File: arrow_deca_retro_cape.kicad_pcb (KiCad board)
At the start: 4 copper layers, 78.6 x 100 mm, 30 parts, among them J1 ZXSP_ED2X28_SPE_SOL_EDGE, J10 Conn_02x05_Odd_Even, J12 Conn_01x03, J13 Conn_01x01, J14 Conn_01x02, J15 Conn_01x03, J16 Conn_01x06, J2 Conn_01x03, J4 DB9_Male, J5 DINC_MIN_TM_6_1, J6 Conn_02x20_Odd_Even, J7 Conn_01x03, J8 P8_Male, J9 P9_Male, U4 LM1117-3.3, U5 LM1117-2.5

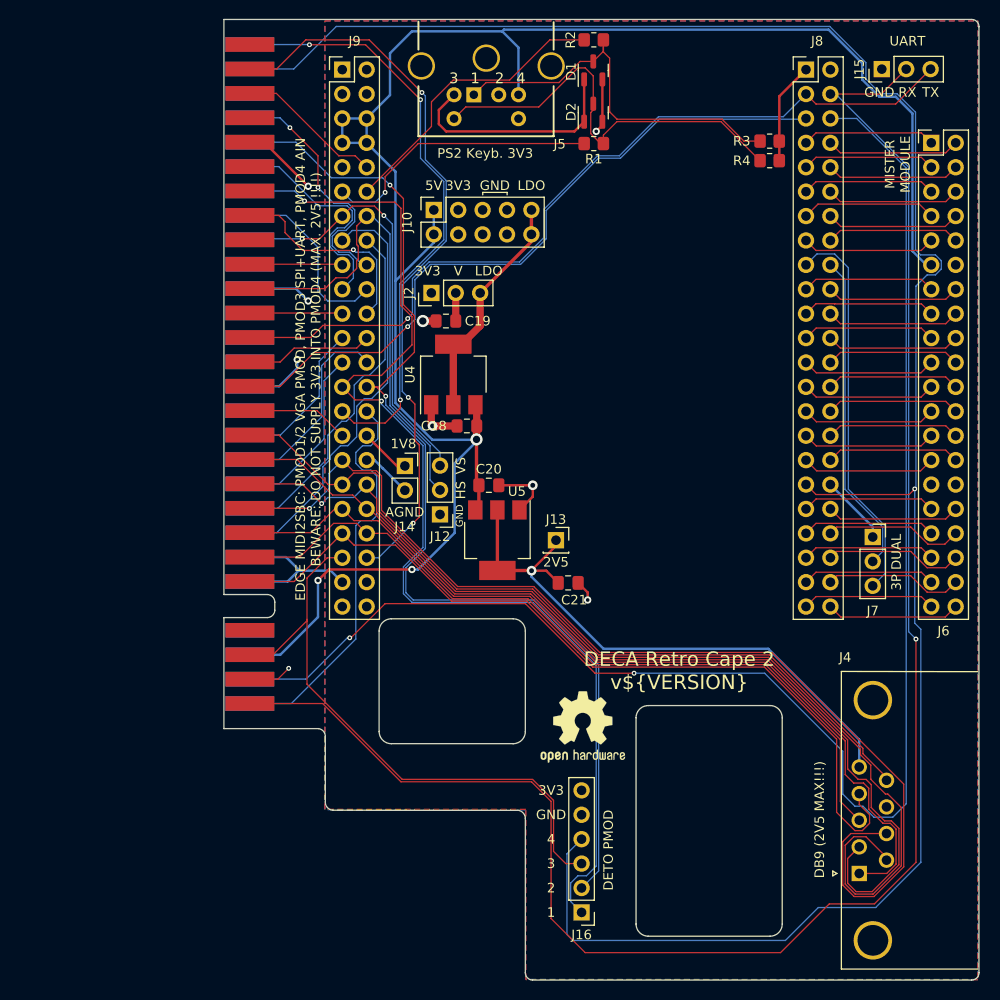
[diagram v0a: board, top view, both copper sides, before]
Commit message: v0.61 2-layer. Edge removed
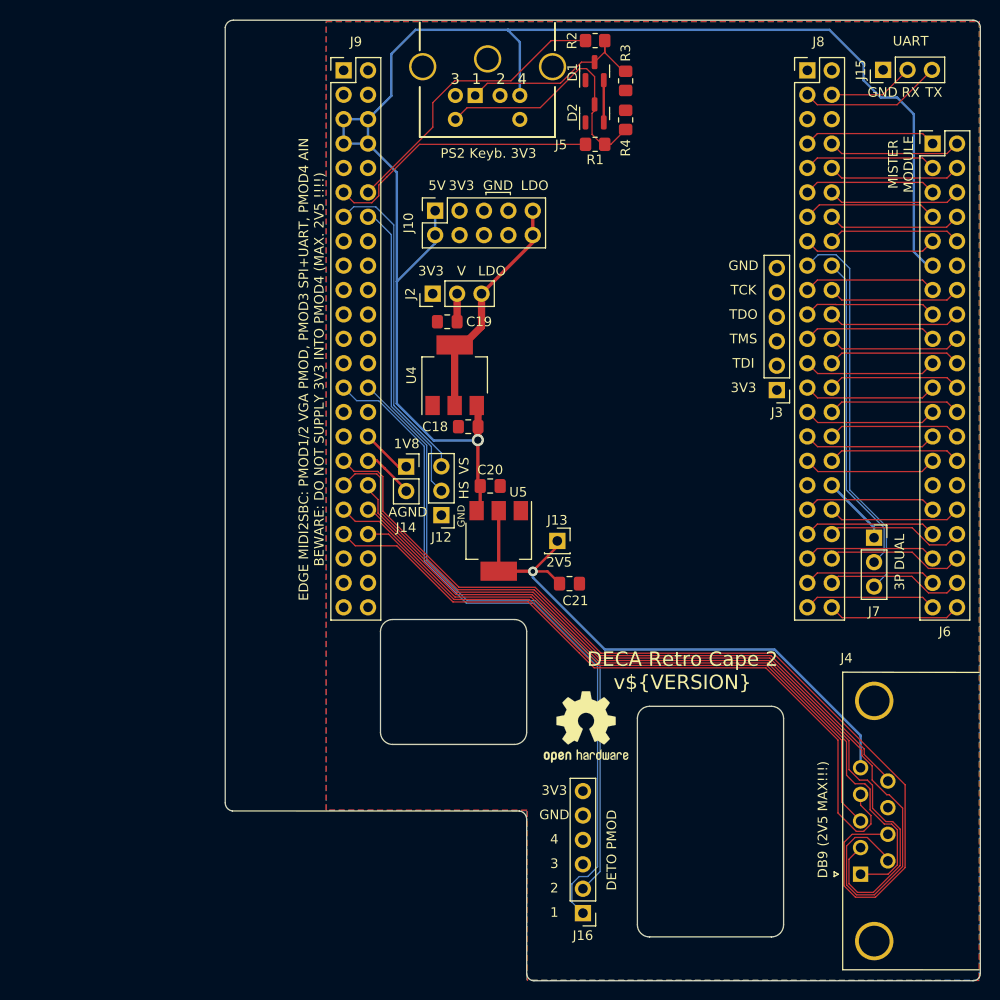
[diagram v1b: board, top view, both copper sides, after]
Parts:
- removed J1: ZXSP_ED2X28_SPE_SOL_EDGE, addon-edge-rpi-i2s-pmod:2X28_SPE2
- added J3: Conn_01x06, Connector_PinHeader_2.54mm:PinHeader_1x06_P2.54mm_Vertical, F.Cu at (161.9, 79.0)
- moved R3 16.2 mm to (146.2, 46.8), turned to -90 degrees
- moved R4 15.6 mm to (146.2, 50.9), turned to 90 degrees
- moved LO2 0.34 mm to (142.1, 114.0)
- moved C21 0.16 mm to (140.3, 99.1)
- moved J13 0.16 mm to (139.1, 94.7)
- moved J16 0.16 mm to (141.7, 133.4)
- moved C19 0.16 mm to (127.6, 71.9)
- moved J10 0.16 mm to (126.4, 60.3)
- moved J12 0.16 mm to (127.0, 92.0)
- moved J14 0.16 mm to (123.4, 87.0)
- moved J2 0.16 mm to (126.1, 69.0)
- moved J9 0.16 mm to (116.8, 45.7)
- moved C18 0.16 mm to (129.8, 82.8)
- moved C20 0.16 mm to (132.1, 89.0)
- moved D1 0.16 mm to (143.0, 45.8)
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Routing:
- net GND: track 477.2 -> 0.00 mm, vias 5 -> 0
- net /DETO4: track 220.8 -> 0.00 mm, vias 1 -> 0
- net /UART_RXD: track 184.0 -> 8.96 mm, vias 1 -> 0
- net /SPI_CS_IO: track 160.1 -> 0.00 mm, vias 2 -> 0
- net +3V3: track 159.8 -> 7.32 mm, vias 2 -> 0
- net /SPI_CS_FPGA: track 76.5 -> 0.00 mm, vias 3 -> 0
- net /SPI_CS_OSD: track 73.6 -> 0.00 mm, vias 1 -> 0
- net /UART_TXD: track 87.1 -> 14.9 mm, vias 1 -> 0
- net +2V5: track 130.6 -> 62.3 mm, vias 2 -> 1
- net /DETO3: track 62.6 -> 0.00 mm
- net /SPI_DI (MISO): track 62.3 -> 0.00 mm, vias 3 -> 0
- net /PS2_MOUSE_DAT: track 61.0 -> 0.00 mm, vias 1 -> 0
- net /DETO2: track 113.9 -> 67.1 mm, vias 2 -> 0
- net /DETO1: track 118.6 -> 73.2 mm, vias 2 -> 0
- net /VGA_B0: track 44.3 -> 0.00 mm
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- removed copper zone on In2.Cu, net +3V3
- removed copper zone on In1.Cu, net GND
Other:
- outline, holes or cut-outs redrawn
- copper layers 4 -> 2
- board text added: "TCK"
- board text added: "TDI"
- board text added: "TDO"
- board text added: "TMS"
- board text added: "https://github.com/somhi/DECA_retro_cape_2"
- board text removed: "0.1270 mm"
- board text removed: "0.1270 mm / 0.0000 mm"
- board text removed: "1.6000 mm"
- board text removed: "78.6332 mm x 100.0130 mm"
- board text removed: "BOARD CHARACTERISTICS"
- board text removed: "Board Thickness:"
- board text removed: "Board overall dimensions:"
- board text removed: "Castellated pads:"
- board text removed: "Copper Finish:"
- board text removed: "Copper Layer Count:"
- board text removed: "DECA Retro Cape 1 v${VERSION}"
- board text removed: "Edge card connectors:"
- board text removed: "Impedance Control:"
- board text removed: "Min hole diameter:"
- board text removed: "Min track/spacing:"
- board text removed: "No"
- board text removed: "None"
- board text removed: "Plated Board Edge:"
- board text removed: "https://github.com/somhi/DECA_retro_cape_1"

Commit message: v0.62 only vga routing missing
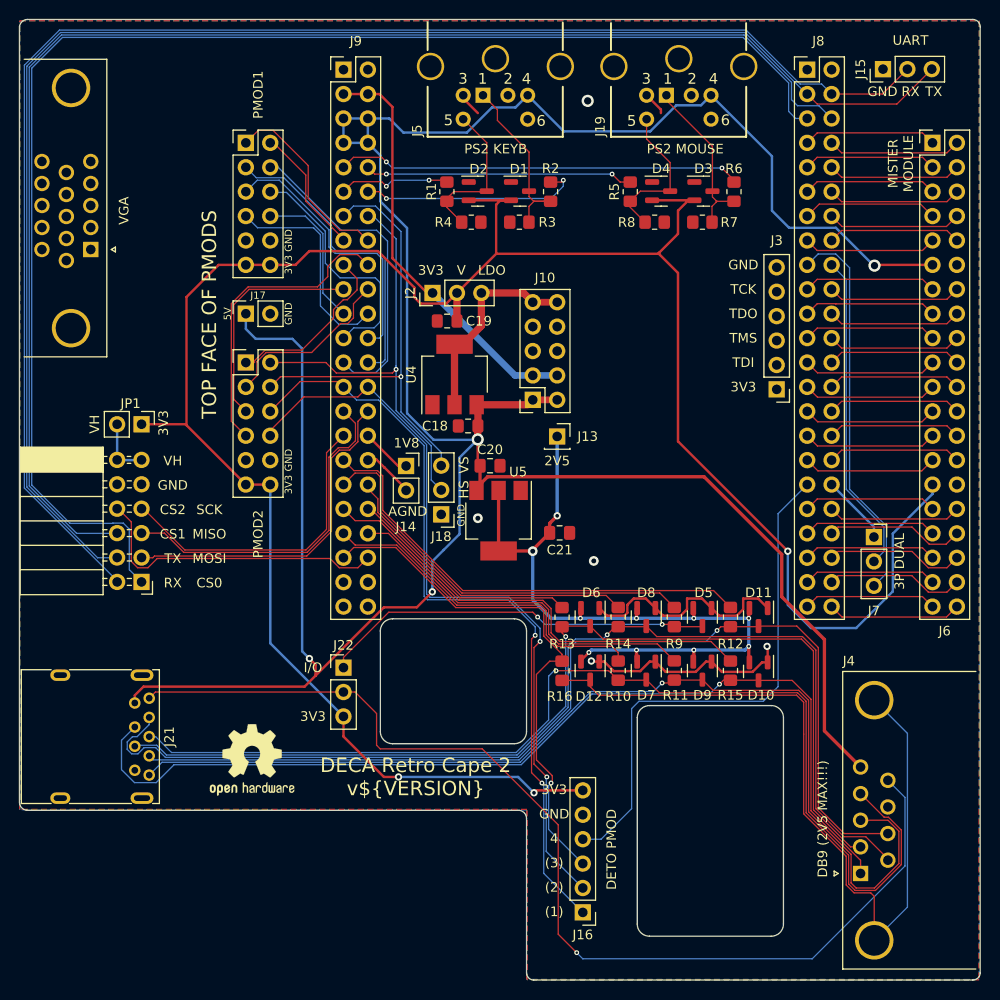
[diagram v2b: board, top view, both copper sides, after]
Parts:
- added D10: BAT54S, Package_TO_SOT_SMD:SOT-23, F.Cu at (160.0, 108.3)
- added D11: BAT54S, Package_TO_SOT_SMD:SOT-23, F.Cu at (160.0, 102.6)
- added D12: BAT54S, Package_TO_SOT_SMD:SOT-23, F.Cu at (142.5, 108.2)
- added D3: BAT54S, Package_TO_SOT_SMD:SOT-23, F.Cu at (154.3, 58.3)
- added D4: BAT54S, Package_TO_SOT_SMD:SOT-23, F.Cu at (149.9, 58.3)
- added D5: BAT54S, Package_TO_SOT_SMD:SOT-23, F.Cu at (154.2, 102.6)
- added D6: BAT54S, Package_TO_SOT_SMD:SOT-23, F.Cu at (142.5, 102.6)
- added D7: BAT54S, Package_TO_SOT_SMD:SOT-23, F.Cu at (148.3, 108.2)
- added D8: BAT54S, Package_TO_SOT_SMD:SOT-23, F.Cu at (148.3, 102.6)
- added D9: BAT54S, Package_TO_SOT_SMD:SOT-23, F.Cu at (154.2, 108.2)
- added J1: DB15_Female_HighDensity, vga:DSUB-15-HD_Female_Horizontal_P2.29x2.54mm_EdgePinOffset3.03mm_Housed_MountingHolesOffset4.94mm, F.Cu at (90.5, 64.4)
- added J11: PMOD1, addon-edge-rpi-i2s-pmod:Pmod_2x06_P2.54mm_Vertical_2, F.Cu at (106.7, 53.3)
- added J12: PMOD2, addon-edge-rpi-i2s-pmod:Pmod_2x06_P2.54mm_Vertical_2, F.Cu at (106.7, 76.1)
- added J17: Conn_01x02, Connector_PinSocket_2.54mm:PinSocket_1x02_P2.54mm_Vertical, F.Cu at (106.7, 71.0)
- added J19: DINC_MIN_TM_6_1, ps2:DINC_MIN_TM_6_1PRIMARY, F.Cu at (151.7, 39.8)
- added J20: PMOD3, addon-edge-rpi-i2s-pmod:PMOD_Female_Horizontal_2, F.Cu at (95.8, 86.3)
- added J21: USB3_A, Connector_USB:USB3_A_Molex_48393-001, F.Cu at (95.1, 111.6)
- added J22: Conn_01x03, Connector_PinHeader_2.54mm:PinHeader_1x03_P2.54mm_Vertical, F.Cu at (116.8, 107.9)
- added JP1: Conn_01x02, Connector_PinHeader_2.54mm:PinHeader_1x02_P2.54mm_Vertical, F.Cu at (95.8, 82.5)
- added R10: 100, Resistor_SMD:R_0805_2012Metric_Pad1.20x1.40mm_HandSolder, F.Cu at (145.4, 108.2)
- added R11: 100, Resistor_SMD:R_0805_2012Metric_Pad1.20x1.40mm_HandSolder, F.Cu at (151.3, 108.2)
- added R12: 100, Resistor_SMD:R_0805_2012Metric_Pad1.20x1.40mm_HandSolder, F.Cu at (157.1, 102.6)
- added R13: 100, Resistor_SMD:R_0805_2012Metric_Pad1.20x1.40mm_HandSolder, F.Cu at (139.6, 102.6)
- added R14: 100, Resistor_SMD:R_0805_2012Metric_Pad1.20x1.40mm_HandSolder, F.Cu at (145.4, 102.6)
- added R15: 100, Resistor_SMD:R_0805_2012Metric_Pad1.20x1.40mm_HandSolder, F.Cu at (157.1, 108.2)
- added R16: 100, Resistor_SMD:R_0805_2012Metric_Pad1.20x1.40mm_HandSolder, F.Cu at (139.6, 108.2)
- added R5: 120, Resistor_SMD:R_0805_2012Metric_Pad1.20x1.40mm_HandSolder, F.Cu at (146.7, 58.3)
- added R6: 120, Resistor_SMD:R_0805_2012Metric_Pad1.20x1.40mm_HandSolder, F.Cu at (157.5, 58.3)
- added R7: DNI, Resistor_SMD:R_0805_2012Metric_Pad1.20x1.40mm_HandSolder, F.Cu at (154.2, 61.5)
- added R8: DNI, Resistor_SMD:R_0805_2012Metric_Pad1.20x1.40mm_HandSolder, F.Cu at (149.2, 61.5)
- added R9: 100, Resistor_SMD:R_0805_2012Metric_Pad1.20x1.40mm_HandSolder, F.Cu at (151.3, 102.6)
- J4: value DB9_Male -> DB9_Male_MountingHoles
- R1, R2: value 120 -> 100
- R3, R4: value NC -> DNI
- moved LO3 37.0 mm to (106.7, 108.6)
- moved LO2 34.9 mm to (107.3, 117.5)
- moved LO4 30.2 mm to (89.5, 114.3)
- moved J10 22.2 mm to (136.5, 80.0), turned to 180 degrees
- moved R4 19.3 mm to (130.1, 61.5), turned to 0 degrees
- moved R3 18.4 mm to (135.1, 61.5), turned to 180 degrees
- moved LO1 16.5 mm to (143.3, 58.4)
- moved R2 16.4 mm to (138.4, 58.3), turned to -90 degrees
- moved R1 16.2 mm to (127.6, 58.3), turned to -90 degrees
- moved D1 14.7 mm to (135.2, 58.3), turned to 0 degrees
- moved D2 14.6 mm to (130.8, 58.3), turned to 0 degrees
- moved J13 10.9 mm to (139.1, 83.8)
- moved C21 5.38 mm to (139.3, 93.9)
- moved C20 2.11 mm to (132.1, 86.9)
- moved U5 2.11 mm to (133.0, 92.6)
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- renumbered J12 to J18
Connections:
- net /DETO3 renamed /JOY_MUX_DETO3
- J4 pad 0: (no net) -> /MUX
- J4 pad 1: /JOY1_UP -> /D-
- J4 pad 2: /JOY1_DOWN -> /D+
- J4 pad 3: /JOY1_LEFT -> /RX-
- J4 pad 4: /JOY1_RIGHT -> /DRAIN
- J4 pad 5: +2V5 -> +5V
- J4 pad 6: /JOY1_B1_P6 -> /TX-
- J4 pad 7: /JOYX_SEL_O -> /RX+
- J4 pad 9: /JOY1_B2_P9 -> /TX+
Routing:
- net +3V3: track 7.32 -> 236.6 mm, vias 0 -> 3
- net /SPI_CS_OSD: track 0.00 -> 148.7 mm
- net /UART_RXD: track 8.96 -> 155.1 mm
- net /SPI_CS_IO: track 0.00 -> 144.5 mm
- net /UART_TXD: track 14.9 -> 156.7 mm
- net +5V: track 160.9 -> 299.3 mm, vias 1 -> 4
- net /TX-: track 0.00 -> 113.8 mm, vias 0 -> 1
- net /DRAIN: track 0.00 -> 113.7 mm, vias 0 -> 1
- net /TX+: track 0.00 -> 112.7 mm, vias 0 -> 1
- net /RX-: track 0.00 -> 108.5 mm, vias 0 -> 1
- net /D+: track 0.00 -> 106.1 mm, vias 0 -> 1
- net /RX+: track 0.00 -> 105.2 mm, vias 0 -> 1
- net /D-: track 0.00 -> 102.8 mm, vias 0 -> 1
- net /MUX: track 0.00 -> 83.3 mm
- net /JOY1_B1_P6: track 95.3 -> 32.4 mm
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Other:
- board size 78.6 x 100 mm -> 100 x 100 mm
- board text added: "(1)"
- board text added: "(2)"
- board text added: "(3)"
- board text added: "0.1270 mm"
- board text added: "0.1270 mm / 0.0000 mm"
- board text added: "0.5700 mm"
- board text added: "100.0332 mm x 100.0130 mm"
- board text added: "BOARD CHARACTERISTICS"
- board text added: "Board Thickness:"
- board text added: "Board overall dimensions:"
- board text added: "CS0"
- board text added: "CS1"
- board text added: "CS2"
- board text added: "Castellated pads:"
- board text added: "Copper Finish:"
- board text added: "Copper Layer Count:"
- board text added: "Edge card connectors:"
- board text added: "I/O"
- board text added: "Impedance Control:"
- board text added: "MISO"
- board text added: "MOSI"
- board text added: "Min hole diameter:"
- board text added: "Min track/spacing:"
- board text added: "No"
- board text added: "None"
- board text added: "PMOD1"
- board text added: "PMOD2"
- board text added: "PS2 KEYB"
- board text added: "PS2 MOUSE"
- board text added: "Plated Board Edge:"
- board text added: "SCK"
- board text added: "TOP FACE OF PMODS"
- board text added: "VGA"
- board text added: "VH"
- board text removed: "1"
- board text removed: "3"
- board text removed: "EDGE MIDI2SBC: PMOD1/2 VGA PMOD, PMOD3 SPI+UART, PMOD4 AIN BEWARE: DO NOT SUPPLY 3V3 INTO PMOD4 (MAX. 2V5 !!!!)"
- board text removed: "PS2 Keyb. 3V3"

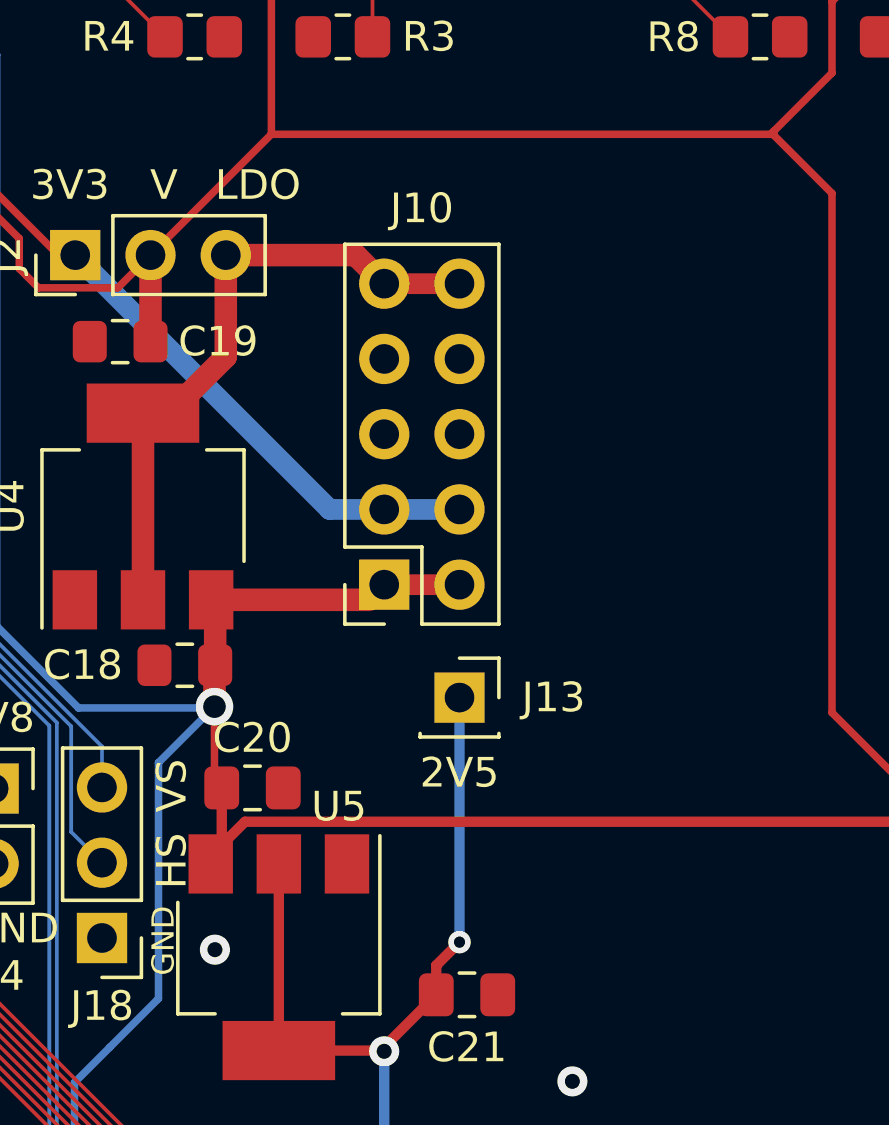
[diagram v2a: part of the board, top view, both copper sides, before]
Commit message: v0.62 final without vga
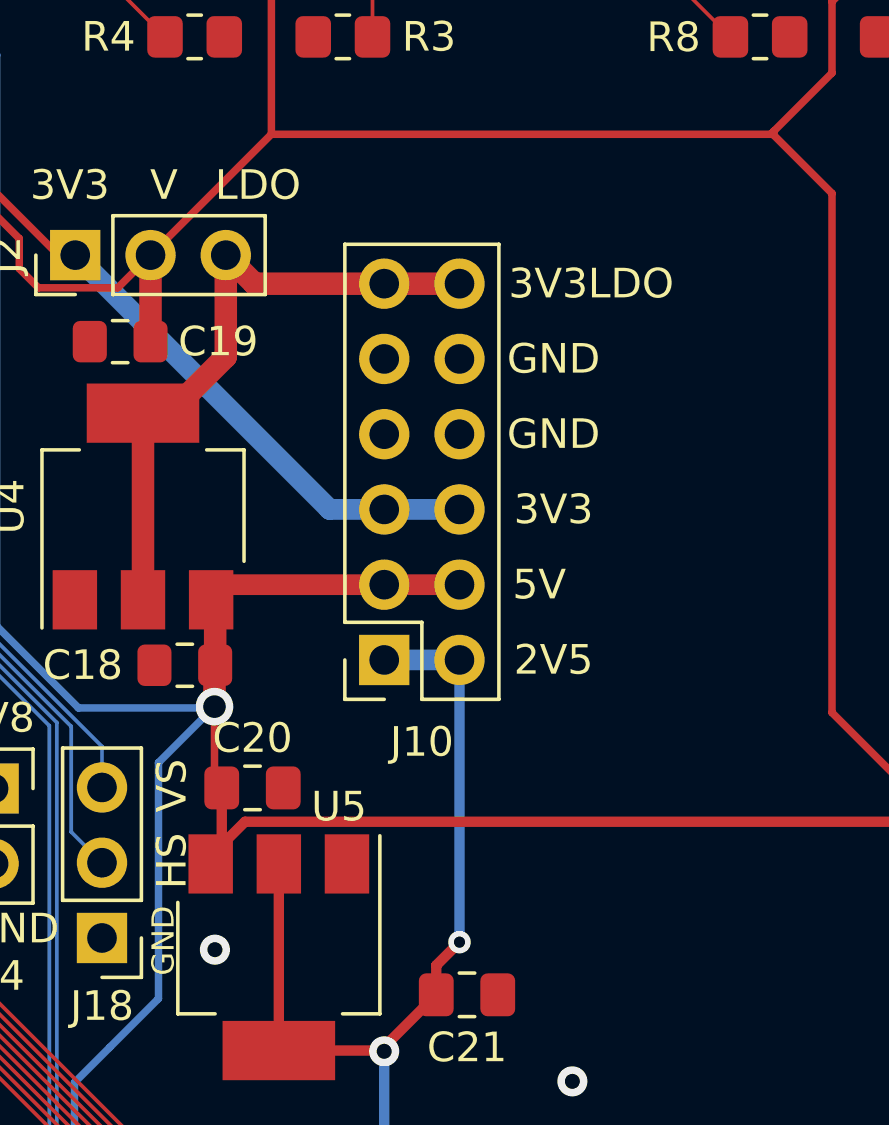
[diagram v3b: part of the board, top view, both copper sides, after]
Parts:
- removed J13: Conn_01x01, Connector_PinSocket_2.54mm:PinSocket_1x01_P2.54mm_Vertical
- J10: value Conn_02x05_Odd_Even -> Conn_02x06_Odd_Even; footprint Connector_PinSocket_2.54mm:PinSocket_2x05_P2.54mm_Vertical -> Connector_PinSocket_2.54mm:PinSocket_2x06_P2.54mm_Vertical
- moved J10 2.54 mm to (136.5, 82.5)
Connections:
- J10 pad 1: +5V -> +2V5
- J10 pad 10: /3V3_LDO -> GND
- J10 pad 2: +5V -> +2V5
- J10 pad 3: +3.3VP -> +5V
- J10 pad 4: +3.3VP -> +5V
- J10 pad 5: GND -> +3.3VP
- J10 pad 6: GND -> +3.3VP
- J10 pad 9: /3V3_LDO -> GND
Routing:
- net +2V5: track 80.8 -> 84.7 mm
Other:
- board text added: "3V3LDO"
